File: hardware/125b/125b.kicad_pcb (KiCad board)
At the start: 2 copper layers, 59 x 75 mm, 58 parts, among them J1 Guitar in, J10 Barrel_Jack, J11 NRJ6HF, J2 fsw pin 7, J3 fsw pin 2, J4 fsw pin 7, J5 fsw pin 5, J6 fsw pin 6, J7 fsw pin 3, J8 fsw pin 4, J9 fsw pin 1, SW1 Switch 1, SW2 Switch 2, SW3 RotaryEncoder_Switch, SW4 SW_DIP_x02, U1 TL074, U2 L78L05_TO92

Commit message: Start work on SMD caps and resistors
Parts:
- removed the J2 at (134.0, 44.0)
- removed J5: fsw pin 5, Connector_Wire:SolderWire-0.25sqmm_1x01_D0.65mm_OD2mm
- removed J6: fsw pin 6, Connector_Wire:SolderWire-0.25sqmm_1x01_D0.65mm_OD2mm
- removed J7: fsw pin 3, Connector_Wire:SolderWire-0.25sqmm_1x01_D0.65mm_OD2mm
- removed J8: fsw pin 4, Connector_Wire:SolderWire-0.25sqmm_1x01_D0.65mm_OD2mm
- removed J9: fsw pin 1, Connector_Wire:SolderWire-0.25sqmm_1x01_D0.65mm_OD2mm
- C10: renamed from C7; footprint Capacitor_THT:C_Rect_L7.0mm_W2.5mm_P5.00mm -> Capacitor_SMD:C_0805_2012Metric
- C11: renamed from C9; footprint Capacitor_THT:C_Rect_L7.0mm_W2.5mm_P5.00mm -> Capacitor_SMD:C_0805_2012Metric
- C12: renamed from C10; footprint Capacitor_THT:C_Rect_L7.0mm_W2.5mm_P5.00mm -> Capacitor_SMD:C_0805_2012Metric
- C2: renamed from C3; footprint Capacitor_THT:C_Rect_L7.0mm_W2.5mm_P5.00mm -> Capacitor_SMD:C_0805_2012Metric
- C3: renamed from C2; footprint Capacitor_THT:C_Rect_L7.0mm_W2.5mm_P5.00mm -> Capacitor_SMD:C_0805_2012Metric
- C4, C5, C6, C8: footprint Capacitor_THT:C_Rect_L7.0mm_W2.5mm_P5.00mm -> Capacitor_SMD:C_0805_2012Metric
- C7: renamed from C11; footprint Capacitor_THT:C_Rect_L7.0mm_W2.5mm_P5.00mm -> Capacitor_SMD:C_0805_2012Metric
- C9: renamed from C12; footprint Capacitor_THT:C_Rect_L7.0mm_W2.5mm_P5.00mm -> Capacitor_SMD:C_0805_2012Metric
- J3: value fsw pin 2 -> Conn_02x05_Odd_Even_MountingPin; footprint Connector_Wire:SolderWire-0.25sqmm_1x01_D0.65mm_OD2mm -> Connector_IDC:IDC-Header_2x05_P2.54mm_Vertical; moved to F.Cu
- J4: value fsw pin 7 -> NRJ6HF; footprint Connector_Wire:SolderWire-0.25sqmm_1x01_D0.65mm_OD2mm -> Connector_Audio:Jack_6.35mm_Neutrik_NRJ6HF_Horizontal
- R1: footprint Resistor_THT:R_Axial_DIN0207_L6.3mm_D2.5mm_P10.16mm_Horizontal -> Resistor_SMD:R_1206_3216Metric
- R10: renamed from R8; footprint Resistor_THT:R_Axial_DIN0207_L6.3mm_D2.5mm_P10.16mm_Horizontal -> Resistor_SMD:R_0805_2012Metric
- R11: renamed from R9; footprint Resistor_THT:R_Axial_DIN0207_L6.3mm_D2.5mm_P10.16mm_Horizontal -> Resistor_SMD:R_0805_2012Metric
- R12: renamed from R10; footprint Resistor_THT:R_Axial_DIN0207_L6.3mm_D2.5mm_P10.16mm_Horizontal -> Resistor_SMD:R_0805_2012Metric
- R13: renamed from R11; footprint Resistor_THT:R_Axial_DIN0207_L6.3mm_D2.5mm_P10.16mm_Horizontal -> Resistor_SMD:R_0805_2012Metric
- R14: renamed from R12; footprint Resistor_THT:R_Axial_DIN0207_L6.3mm_D2.5mm_P10.16mm_Horizontal -> Resistor_SMD:R_0805_2012Metric
- R15: renamed from R13; footprint Resistor_THT:R_Axial_DIN0207_L6.3mm_D2.5mm_P10.16mm_Horizontal -> Resistor_SMD:R_0805_2012Metric
- R16: renamed from R14; footprint Resistor_THT:R_Axial_DIN0207_L6.3mm_D2.5mm_P10.16mm_Horizontal -> Resistor_SMD:R_0805_2012Metric
- R17: renamed from R5; footprint Resistor_THT:R_Axial_DIN0207_L6.3mm_D2.5mm_P10.16mm_Horizontal -> Resistor_SMD:R_0805_2012Metric
- R18: renamed from R6; footprint Resistor_THT:R_Axial_DIN0207_L6.3mm_D2.5mm_P10.16mm_Horizontal -> Resistor_SMD:R_0805_2012Metric
- R19: renamed from R16; footprint Resistor_THT:R_Axial_DIN0207_L6.3mm_D2.5mm_P10.16mm_Horizontal -> Resistor_SMD:R_0805_2012Metric
- R2, R3, R4: footprint Resistor_THT:R_Axial_DIN0207_L6.3mm_D2.5mm_P10.16mm_Horizontal -> Resistor_SMD:R_0805_2012Metric
- R20: renamed from R15; footprint Resistor_THT:R_Axial_DIN0207_L6.3mm_D2.5mm_P10.16mm_Horizontal -> Resistor_SMD:R_0805_2012Metric
- R21: renamed from R17; footprint Resistor_THT:R_Axial_DIN0207_L6.3mm_D2.5mm_P10.16mm_Horizontal -> Resistor_SMD:R_0805_2012Metric
- R22: renamed from R18; footprint Resistor_THT:R_Axial_DIN0207_L6.3mm_D2.5mm_P10.16mm_Horizontal -> Resistor_SMD:R_0805_2012Metric
- R5: renamed from R19; footprint Resistor_THT:R_Axial_DIN0207_L6.3mm_D2.5mm_P10.16mm_Horizontal -> Resistor_SMD:R_0805_2012Metric
- R6: renamed from R20; footprint Resistor_THT:R_Axial_DIN0207_L6.3mm_D2.5mm_P10.16mm_Horizontal -> Resistor_SMD:R_0805_2012Metric
- R7: renamed from R21; footprint Resistor_THT:R_Axial_DIN0207_L6.3mm_D2.5mm_P10.16mm_Horizontal -> Resistor_SMD:R_0805_2012Metric
- R8: renamed from R22; footprint Resistor_THT:R_Axial_DIN0207_L6.3mm_D2.5mm_P10.16mm_Horizontal -> Resistor_SMD:R_0805_2012Metric
- R9: renamed from R7; footprint Resistor_THT:R_Axial_DIN0207_L6.3mm_D2.5mm_P10.16mm_Horizontal -> Resistor_SMD:R_0805_2012Metric
- moved J3 19.9 mm to (119.8, 127.8)
- renumbered J10 to J2, J11 to J4, SW4 to SW1, SW3 to SW2, SW1 to SW3, SW2 to SW4, U2 to U1, U1 to U2
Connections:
- C11 pad 2: Net-(J7-Pin_1) -> /fsw3
- C12 pad 2: Net-(J9-Pin_1) -> /fsw1
- D1 pad 1: Net-(D1-K) -> /fsw2
- J1 pad T: Net-(J2-Pin_1) -> /fsw7
- J3 pad 1: Net-(D1-K) -> /fsw1
- J4 pad R: Net-(J6-Pin_1) -> /fsw6
- J4 pad RN: unconnected-(J11-PadRN) -> unconnected-(J4-PadRN)
- J4 pad SN: unconnected-(J11-PadSN) -> unconnected-(J4-PadSN)
- J4 pad T: Net-(J8-Pin_1) -> /fsw4
- J4 pad TN: unconnected-(J11-PadTN) -> unconnected-(J4-PadTN)
- R21 pad 1: Net-(J7-Pin_1) -> /fsw3
- R22 pad 1: Net-(J9-Pin_1) -> /fsw1
- SW1 pad 1: Net-(J4-Pin_1) -> /fsw7
- SW1 pad 2: Net-(J4-Pin_1) -> /fsw7
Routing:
- net GND: track 157.7 -> 0.00 mm
- net /VCC: track 118.2 -> 0.00 mm, vias 1 -> 0
- net /3v3: track 105.5 -> 0.00 mm, vias 1 -> 0
- net Net-(D2-A): track 89.1 -> 0.00 mm
- net /ENC_A: track 87.8 -> 0.00 mm, vias 3 -> 0
- net Net-(U2B-+): track 83.6 -> 0.00 mm, vias 1 -> 0
- net Net-(U2A-+): track 76.7 -> 0.00 mm, vias 1 -> 0
- net +5V: track 73.8 -> 0.00 mm
- net Net-(C10-Pad1): track 70.8 -> 0.00 mm
- net /Left out: track 54.9 -> 0.00 mm, vias 3 -> 0
- net Net-(A1-ADC_6): track 54.5 -> 0.00 mm, vias 1 -> 0
- net Net-(U2C-+): track 52.0 -> 0.00 mm
- net Net-(U2B--): track 41.3 -> 0.00 mm, vias 1 -> 0
- net Net-(C3-Pad1): track 39.5 -> 0.00 mm
- net Net-(A1-ADC_0): track 36.6 -> 0.00 mm
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- removed copper zone on B.Cu, net GND
- removed copper zone on F.Cu, net GND

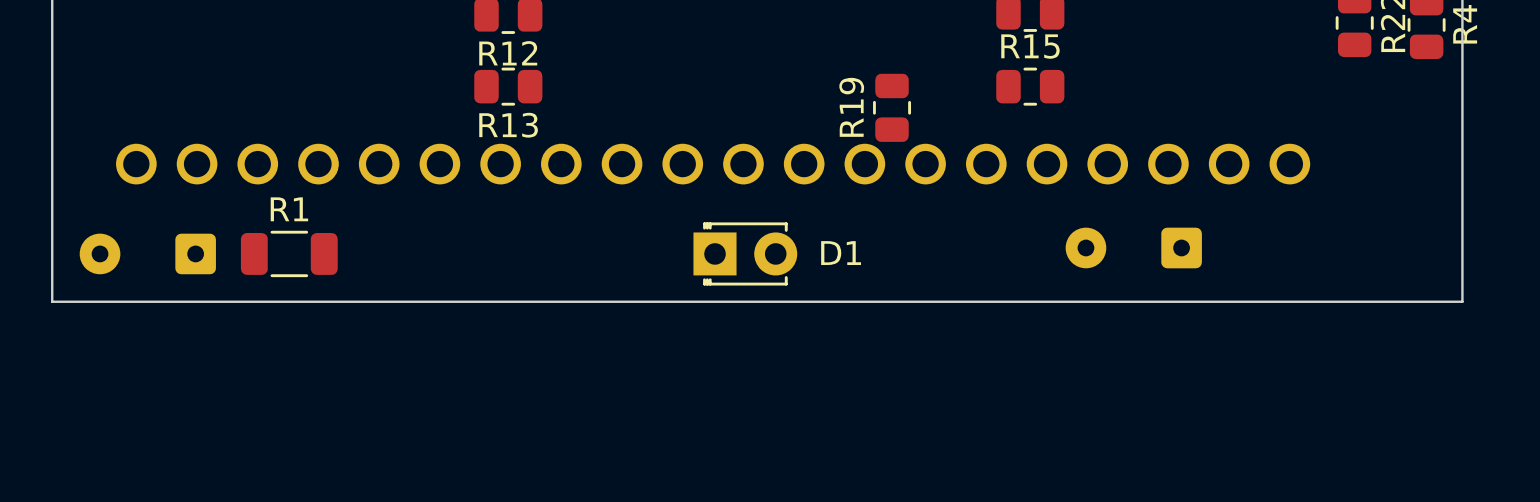
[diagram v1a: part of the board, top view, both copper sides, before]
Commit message: Increase size of holes for switch connectors
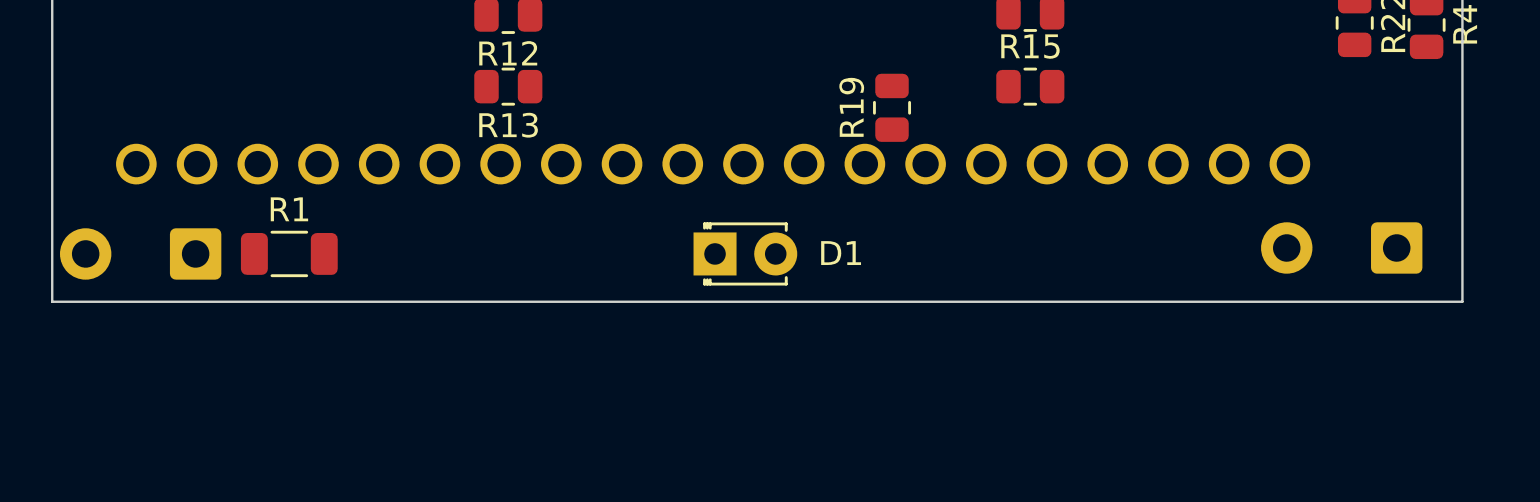
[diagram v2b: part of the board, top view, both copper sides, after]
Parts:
- SW3, SW4: footprint Connector_Wire:SolderWire-0.15sqmm_1x02_P4mm_D0.5mm_OD1.5mm -> Connector_Wire:SolderWire-0.5sqmm_1x02_P4.6mm_D0.9mm_OD2.1mm
- moved SW4 9.00 mm to (154.2, 107.8)
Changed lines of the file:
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@@
 		)
 	)
-	(footprint "Connector_Wire:SolderWire-0.15sqmm_1x02_P4mm_D0.5mm_OD1.5mm"
+	(footprint "Connector_Wire:SolderWire-0.5sqmm_1x02_P4.6mm_D0.9mm_OD2.1mm"
 		(layer "B.Cu")
 		(at 104 108 180)
-		(descr "Soldered wire connection, for 2 times 0.15 mm² wires, basic insulation, conductor diameter 0.5mm, outer diameter 1.5mm, size source Multi-Contact FLEXI-E 0.15 (https://ec.staubli.com/AcroFiles/Catalogues/TM_Cab-Main-11014119_(en)_hi.pdf), bend radius 3 times outer diameter, generated with kicad-footprint-generator")
-		(tags "connector wire 0.15sqmm")
+		(descr "Soldered wire connection, for 2 times 0.5 mm² wires, basic insulation, conductor diameter 0.9mm, outer diameter 2.1mm, size source Multi-Contact FLEXI-E 0.50 (https://www.staubli.com/content/dam/ecs/catalogs-brochures/TM/CAB-Main-11014119-en.pdf#page=9), bend radius 3 times outer diameter, generated with kicad-footprint-generator")
+		(tags "connector wire 0.5sqmm")
 		(property "Reference" "SW3"
-			(at 2.305213 1.5 0)
+			(at 2.3 2.28 0)
 			(layer "B.SilkS")
 			(effects
@@
 		)
 		(property "Value" "Switch 1"
-			(at 2 -2.05 0)
+			(at 2.3 -2.28 0)
 			(layer "B.Fab")
 			(effects
@@
 		(property "Datasheet" "~"
 			(at 0 0 0)
-			(unlocked yes)
 			(layer "B.Fab")
 			(hide yes)
@@
 		(property "Description" ""
 			(at 0 0 0)
-			(unlocked yes)
 			(layer "B.Fab")
 			(hide yes)
@@
 		(attr exclude_from_pos_files)
 		(fp_line
-			(start 5.5 1.35)
-			(end 2.5 1.35)
-			(stroke
-				(width 0.05)
-				(type solid)
-			)
-			(layer "B.CrtYd")
-		)
-		(fp_line
-			(start 5.5 -1.35)
-			(end 5.5 1.35)
-			(stroke
-				(width 0.05)
-				(type solid)
-			)
-			(layer "B.CrtYd")
-		)
-		(fp_line
-			(start 2.5 1.35)
-			(end 2.5 -1.35)
-			(stroke
-				(width 0.05)
-				(type solid)
-			)
-			(layer "B.CrtYd")
-		)
-		(fp_line
-			(start 2.5 -1.35)
-			(end 5.5 -1.35)
-			(stroke
-				(width 0.05)
-				(type solid)
-			)
-			(layer "B.CrtYd")
-		)
-		(fp_line
-			(start 1.5 1.35)
-			(end -1.5 1.35)
-			(stroke
-				(width 0.05)
-				(type solid)
-			)
-			(layer "B.CrtYd")
-		)
-		(fp_line
-			(start 1.5 -1.35)
-			(end 1.5 1.35)
-			(stroke
-				(width 0.05)
-				(type solid)
-			)
-			(layer "B.CrtYd")
-		)
-		(fp_line
-			(start -1.5 1.35)
-			(end -1.5 -1.35)
-			(stroke
-				(width 0.05)
-				(type solid)
-			)
-			(layer "B.CrtYd")
-		)
-		(fp_line
-			(start -1.5 -1.35)
-			(end 1.5 -1.35)
+			(start 6.4 1.58)
+			(end 2.8 1.58)
+			(stroke
+				(width 0.05)
+				(type solid)
+			)
+			(layer "B.CrtYd")
+		)
+		(fp_line
+			(start 6.4 -1.58)
+			(end 6.4 1.58)
+			(stroke
+				(width 0.05)
+				(type solid)
+			)
+			(layer "B.CrtYd")
+		)
+		(fp_line
+			(start 2.8 1.58)
+			(end 2.8 -1.58)
+			(stroke
+				(width 0.05)
+				(type solid)
+			)
+			(layer "B.CrtYd")
+		)
+		(fp_line
+			(start 2.8 -1.58)
+			(end 6.4 -1.58)
+			(stroke
+				(width 0.05)
+				(type solid)
+			)
+			(layer "B.CrtYd")
+		)
+		(fp_line
+			(start 1.8 1.58)
+			(end -1.8 1.58)
+			(stroke
+				(width 0.05)
+				(type solid)
+			)
+			(layer "B.CrtYd")
+		)
+		(fp_line
+			(start 1.8 -1.58)
+			(end 1.8 1.58)
+			(stroke
+				(width 0.05)
+				(type solid)
+			)
+			(layer "B.CrtYd")
+		)
+		(fp_line
+			(start -1.8 1.58)
+			(end -1.8 -1.58)
+			(stroke
+				(width 0.05)
+				(type solid)
+			)
+			(layer "B.CrtYd")
+		)
+		(fp_line
+			(start -1.8 -1.58)
+			(end 1.8 -1.58)
 			(stroke
 				(width 0.05)
@@
 		)
 		(fp_circle
-			(center 4 0)
-			(end 4.75 0)
+			(center 4.6 0)
+			(end 5.65 0)
 			(stroke
 				(width 0.1)
@@
 		(fp_circle
 			(center 0 0)
-			(end 0.75 0)
+			(end 1.05 0)
 			(stroke
 				(width 0.1)
@@
 		)
 		(fp_text user "${REFERENCE}"
-			(at 2 0 270)
-			(layer "B.Fab")
-			(effects
-				(font
-					(size 0.68 0.68)
-					(thickness 0.1)
+			(at 2.3 0 270)
+			(layer "B.Fab")
+			(effects
+				(font
+					(size 0.79 0.79)
+					(thickness 0.12)
 				)
 				(justify mirror)
@@
 		(pad "1" thru_hole roundrect
 			(at 0 0 180)
-			(size 1.7 1.7)
-			(drill 0.7)
-			(layers "*.Cu" "*.Mask")
-			(remove_unused_layers no)
-			(roundrect_rratio 0.147059)
+			(size 2.15 2.15)
+			(drill 1.15)
+			(layers "*.Cu" "*.Mask")
+			(remove_unused_layers no)
+			(roundrect_rratio 0.116279)
 			(net 34 "Net-(A1-SAI2_FS)")
 			(pinfunction "1")
@@
 		)
 		(pad "2" thru_hole circle
-			(at 4 0 180)
-			(size 1.7 1.7)
-			(drill 0.7)
+			(at 4.6 0 180)
+			(size 2.15 2.15)
+			(drill 1.15)
 			(layers "*.Cu" "*.Mask")
 			(remove_unused_layers no)
@@
 		)
 		(embedded_fonts no)
-		(model "${KICAD6_3DMODEL_DIR}/Connector_Wire.3dshapes/SolderWire-0.15sqmm_1x02_P4mm_D0.5mm_OD1.5mm.wrl"
+		(model "${KICAD9_3DMODEL_DIR}/Connector_Wire.3dshapes/SolderWire-0.5sqmm_1x02_P4.6mm_D0.9mm_OD2.1mm.step"
 			(offset
 				(xyz 0 0 0)
@@
 		)
 	)
-	(footprint "Connector_Wire:SolderWire-0.15sqmm_1x02_P4mm_D0.5mm_OD1.5mm"
+	(footprint "Connector_Wire:SolderWire-0.5sqmm_1x02_P4.6mm_D0.9mm_OD2.1mm"
 		(layer "B.Cu")
-		(at 145.25 107.75 180)
-		(descr "Soldered wire connection, for 2 times 0.15 mm² wires, basic insulation, conductor diameter 0.5mm, outer diameter 1.5mm, size source Multi-Contact FLEXI-E 0.15 (https://ec.staubli.com/AcroFiles/Catalogues/TM_Cab-Main-11014119_(en)_hi.pdf), bend radius 3 times outer diameter, generated with kicad-footprint-generator")
-		(tags "connector wire 0.15sqmm")
+		(at 154.25 107.75 180)
+		(descr "Soldered wire connection, for 2 times 0.5 mm² wires, basic insulation, conductor diameter 0.9mm, outer diameter 2.1mm, size source Multi-Contact FLEXI-E 0.50 (https://www.staubli.com/content/dam/ecs/catalogs-brochures/TM/CAB-Main-11014119-en.pdf#page=9), bend radius 3 times outer diameter, generated with kicad-footprint-generator")
+		(tags "connector wire 0.5sqmm")
 		(property "Reference" "SW4"
-			(at 2.1686 1.7071 0)
+			(at 2.3 2.28 0)
 			(layer "B.SilkS")
 			(effects
@@
 		)
 		(property "Value" "Switch 2"
-			(at 2 -2.05 0)
+			(at 2.3 -2.28 0)
 			(layer "B.Fab")
 			(effects
@@
 		(property "Datasheet" "~"
 			(at 0 0 0)
-			(unlocked yes)
 			(layer "B.Fab")
 			(hide yes)
@@
 		(property "Description" ""
 			(at 0 0 0)
-			(unlocked yes)
 			(layer "B.Fab")
 			(hide yes)
@@
 		(attr exclude_from_pos_files)
 		(fp_line
-			(start 5.5 1.35)
-			(end 2.5 1.35)
-			(stroke
-				(width 0.05)
-				(type solid)
-			)
-			(layer "B.CrtYd")
-		)
-		(fp_line
-			(start 5.5 -1.35)
-			(end 5.5 1.35)
-			(stroke
-				(width 0.05)
-				(type solid)
-			)
-			(layer "B.CrtYd")
-		)
-		(fp_line
-			(start 2.5 1.35)
-			(end 2.5 -1.35)
-			(stroke
-				(width 0.05)
-				(type solid)
-			)
-			(layer "B.CrtYd")
-		)
-		(fp_line
-			(start 2.5 -1.35)
-			(end 5.5 -1.35)
-			(stroke
-				(width 0.05)
-				(type solid)
-			)
-			(layer "B.CrtYd")
-		)
-		(fp_line
-			(start 1.5 1.35)
-			(end -1.5 1.35)
-			(stroke
-				(width 0.05)
-				(type solid)
-			)
-			(layer "B.CrtYd")
-		)
-		(fp_line
-			(start 1.5 -1.35)
-			(end 1.5 1.35)
-			(stroke
-				(width 0.05)
-				(type solid)
-			)
-			(layer "B.CrtYd")
-		)
-		(fp_line
-			(start -1.5 1.35)
-			(end -1.5 -1.35)
-			(stroke
-				(width 0.05)
-				(type solid)
-			)
-			(layer "B.CrtYd")
-		)
-		(fp_line
-			(start -1.5 -1.35)
-			(end 1.5 -1.35)
+			(start 6.4 1.58)
+			(end 2.8 1.58)
+			(stroke
+				(width 0.05)
+				(type solid)
+			)
+			(layer "B.CrtYd")
+		)
+		(fp_line
+			(start 6.4 -1.58)
+			(end 6.4 1.58)
+			(stroke
+				(width 0.05)
+				(type solid)
+			)
+			(layer "B.CrtYd")
+		)
+		(fp_line
+			(start 2.8 1.58)
+			(end 2.8 -1.58)
+			(stroke
+				(width 0.05)
+				(type solid)
+			)
+			(layer "B.CrtYd")
+		)
+		(fp_line
+			(start 2.8 -1.58)
+			(end 6.4 -1.58)
+			(stroke
+				(width 0.05)
+				(type solid)
+			)
+			(layer "B.CrtYd")
+		)
+		(fp_line
+			(start 1.8 1.58)
+			(end -1.8 1.58)
+			(stroke
+				(width 0.05)
+				(type solid)
+			)
+			(layer "B.CrtYd")
+		)
+		(fp_line
+			(start 1.8 -1.58)
+			(end 1.8 1.58)
+			(stroke
+				(width 0.05)
+				(type solid)
+			)
+			(layer "B.CrtYd")
+		)
+		(fp_line
+			(start -1.8 1.58)
+			(end -1.8 -1.58)
+			(stroke
+				(width 0.05)
+				(type solid)
+			)
+			(layer "B.CrtYd")
+		)
+		(fp_line
+			(start -1.8 -1.58)
+			(end 1.8 -1.58)
 			(stroke
 				(width 0.05)
@@
 		)
 		(fp_circle
-			(center 4 0)
-			(end 4.75 0)
+			(center 4.6 0)
+			(end 5.65 0)
 			(stroke
 				(width 0.1)
@@
 		(fp_circle
 			(center 0 0)
-			(end 0.75 0)
+			(end 1.05 0)
 			(stroke
 				(width 0.1)
@@
 		)
 		(fp_text user "${REFERENCE}"
-			(at 2 0 90)
-			(layer "B.Fab")
-			(effects
-				(font
-					(size 0.68 0.68)
-					(thickness 0.1)
+			(at 2.3 0 270)
+			(layer "B.Fab")
+			(effects
+				(font
+					(size 0.79 0.79)
+					(thickness 0.12)
 				)
 				(justify mirror)
@@
 		(pad "1" thru_hole roundrect
 			(at 0 0 180)
-			(size 1.7 1.7)
-			(drill 0.7)
-			(layers "*.Cu" "*.Mask")
-			(remove_unused_layers no)
-			(roundrect_rratio 0.147059)
+			(size 2.15 2.15)
+			(drill 1.15)
+			(layers "*.Cu" "*.Mask")
+			(remove_unused_layers no)
+			(roundrect_rratio 0.116279)
 			(net 35 "Net-(A1-SAI2_SCK)")
 			(pinfunction "1")
@@
 		)
 		(pad "2" thru_hole circle
-			(at 4 0 180)
-			(size 1.7 1.7)
-			(drill 0.7)
+			(at 4.6 0 180)
+			(size 2.15 2.15)
+			(drill 1.15)
 			(layers "*.Cu" "*.Mask")
 			(remove_unused_layers no)
@@
 		)
 		(embedded_fonts no)
-		(model "${KICAD6_3DMODEL_DIR}/Connector_Wire.3dshapes/SolderWire-0.15sqmm_1x02_P4mm_D0.5mm_OD1.5mm.wrl"
+		(model "${KICAD9_3DMODEL_DIR}/Connector_Wire.3dshapes/SolderWire-0.5sqmm_1x02_P4.6mm_D0.9mm_OD2.1mm.step"
 			(offset
 				(xyz 0 0 0)
